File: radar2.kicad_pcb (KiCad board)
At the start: 4 copper layers, 103.4 x 65 mm, 135 parts, among them IC1 BQ25713RSNR, IC2 TPS54540DDA, IC3 LP5907QMFX-3.0Q1, IC5 LP5907QMFX-3.0Q1, IC6 DW3220TR13, J1 GSB1C4621DS1HR, J2 M20-8770546 (for SWD), J3 M20-9730446_DISPLAY_POWER, J4 JST-XH, J5 M20-9990646_PI, J6 SMA_CONNECTOR, J7 SMA_CONNECTOR, Q1 CSD17308Q3, Q2 CSD17308Q3, Q3 CSD17308Q3, Q4 CSD17308Q3, Q5 CSD25404Q3, SW1 09.03290.01, SW2 SWT0220-016016GSA, U1 STM32H725ZETx, Y1 ECS-384-CDX-2482

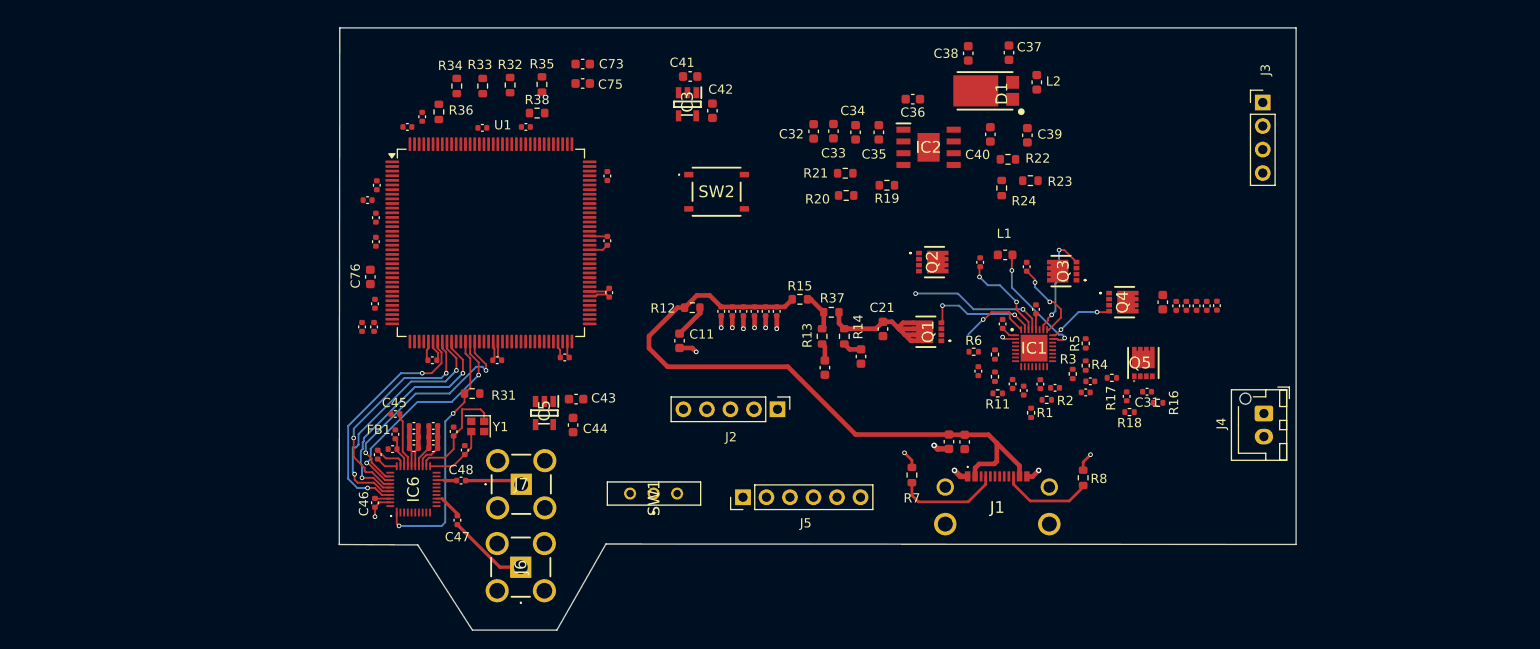
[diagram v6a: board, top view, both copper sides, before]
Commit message: replacing battery charger inductor with the correct one capable of handling high current applications, updating user footprint lib. Doing some serious routing leaving the battery charger for last due to complexity
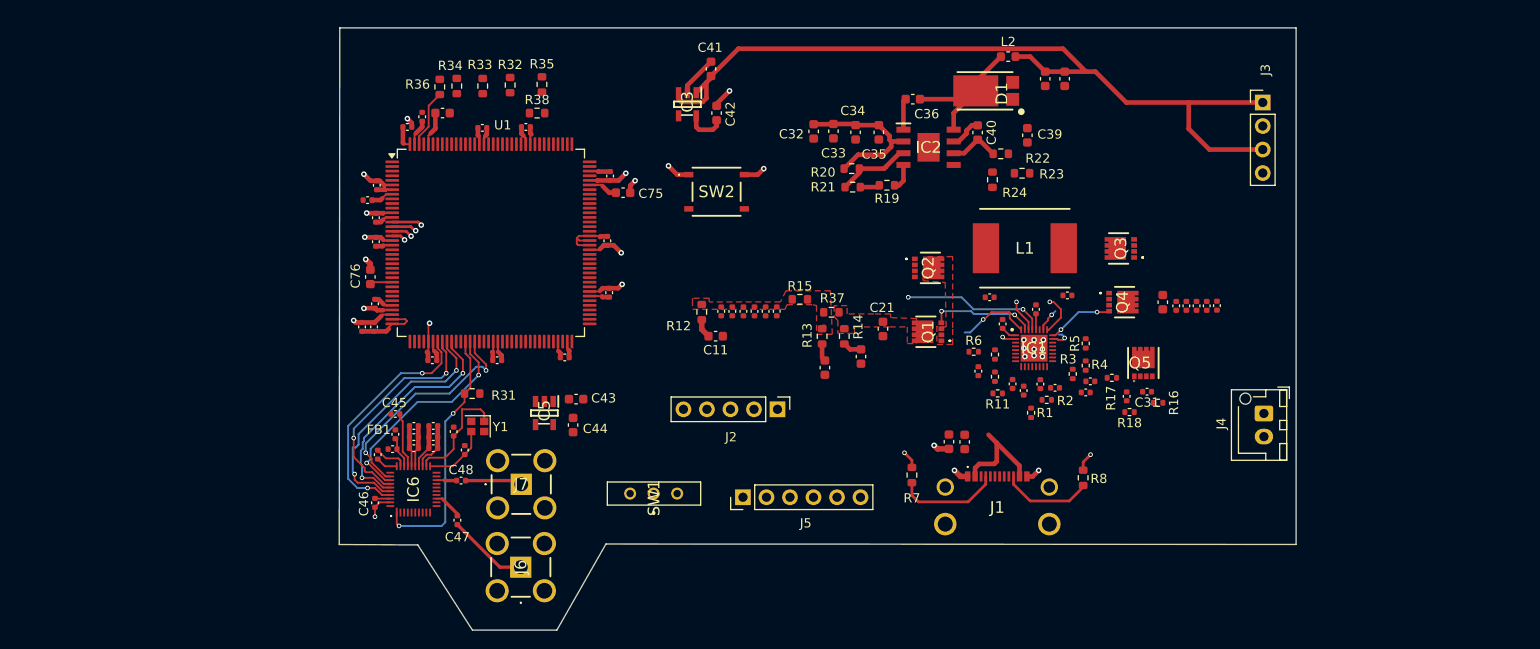
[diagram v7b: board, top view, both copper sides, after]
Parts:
- L1: footprint Inductor_SMD:L_0603_1608Metric -> induct:INDPM9785X300N
- moved C73 16.0 mm to (107.6, 68.0)
- moved C75 12.6 mm to (127.1, 76.6)
- moved C38 8.76 mm to (172.7, 64.3)
- moved Q3 6.69 mm to (180.9, 82.6)
- moved C37 6.64 mm to (174.8, 64.3), turned to 90 degrees
- moved C23 5.38 mm to (175.1, 87.7), turned to 0 degrees
- moved L2 4.15 mm to (168.7, 61.9), turned to 0 degrees
- moved C11 3.93 mm to (137.1, 92.1), turned to 0 degrees
- moved C22 3.92 mm to (166.7, 87.9), turned to 180 degrees
- moved R20 2.96 mm to (151.8, 74.0)
- moved R36 2.70 mm to (107.3, 65.2)
- moved C41 2.40 mm to (136.6, 63.2), turned to -90 degrees
- moved L1 2.24 mm to (170.5, 82.6)
- moved R21 1.70 mm to (151.9, 76.0)
- moved C40 1.39 mm to (165.4, 70.1)
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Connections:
- Q4 pad 5: GND -> /pmics/VSYS
- Q4 pad 6: GND -> /pmics/VSYS
- Q4 pad 7: GND -> /pmics/VSYS
- Q4 pad 8: GND -> /pmics/VSYS
- Q4 pad 9: GND -> /pmics/VSYS
- Q5 pad 5: GND -> /pmics/VSYS
- Q5 pad 6: GND -> /pmics/VSYS
- Q5 pad 7: GND -> /pmics/VSYS
- Q5 pad 8: GND -> /pmics/VSYS
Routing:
- net VOUT_5V: track 0.00 -> 91.4 mm
- net VBUS: track 77.3 -> 13.4 mm
- net GND: track 43.9 -> 93.9 mm, vias 13 -> 34
- net 3V3_MCU: track 10.5 -> 43.3 mm
- net /pmics/VSYS: track 0.00 -> 17.4 mm
- net /pmics/SW_1: track 0.00 -> 16.4 mm
- net Net-(Q1-D_1): track 15.1 -> 0.00 mm
- net /pmics/SW2: track 13.0 -> 2.26 mm, vias 2 -> 1
- net /pmics/LODRV2: track 11.7 -> 2.54 mm, vias 2 -> 1
- net Net-(IC2-EN): track 0.00 -> 8.10 mm
- net Net-(C73-Pad1): track 0.00 -> 6.85 mm
- net Net-(U1-PDR_ON): track 0.00 -> 6.28 mm
- net /pmics/BTST1: track 9.79 -> 3.54 mm, vias 2 -> 1
- net Net-(IC2-COMP): track 0.00 -> 5.50 mm
- net /pmics/BTST2: track 8.83 -> 4.47 mm, vias 2 -> 1
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- added copper zone on F.Cu, net /pmics/SW1
- added copper zone on F.Cu, net Net-(Q1-D_1)
- added copper zone on F.Cu, net VBUS

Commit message: routing power, for mcu and radar, leaving the BQ for lass still
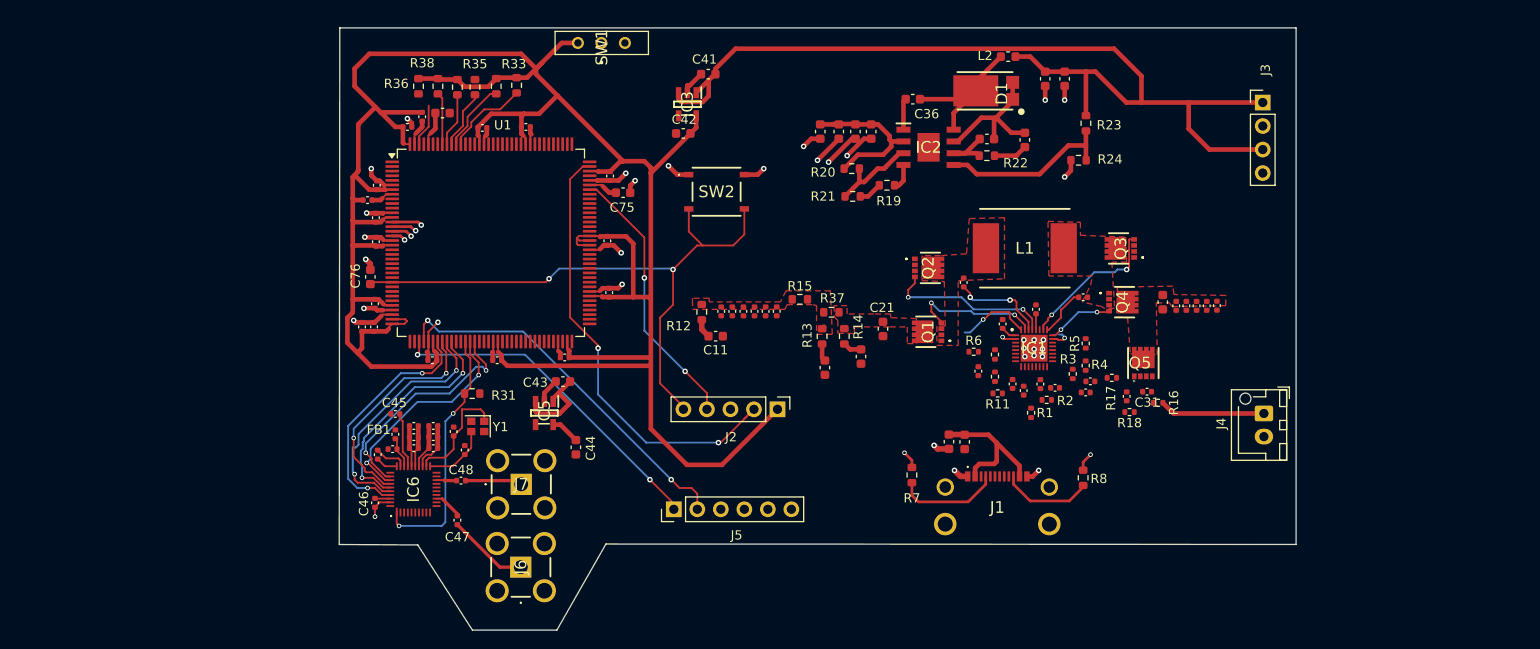
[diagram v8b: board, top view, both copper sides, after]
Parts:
- moved SW1 49.0 mm to (124.8, 60.4)
- moved R38 11.1 mm to (107.1, 65.1), turned to -90 degrees
- moved R24 9.53 mm to (176.3, 73.1), turned to 180 degrees
- moved R23 8.76 mm to (177.1, 69.1), turned to -90 degrees
- moved J5 7.58 mm to (132.6, 110.8)
- moved R35 7.24 mm to (111.1, 65.2)
- moved C42 4.22 mm to (133.6, 70.2), turned to 0 degrees
- moved R33 3.66 mm to (115.6, 65.0)
- moved C22 3.22 mm to (163.9, 86.3), turned to 90 degrees
- moved C44 2.42 mm to (122.0, 104.1), turned to 90 degrees
- moved C43 2.38 mm to (120.6, 97.0), turned to 0 degrees
- moved R36 2.30 mm to (105.0, 65.1)
- moved C23 1.71 mm to (176.8, 87.9)
- moved R22 1.51 mm to (166.4, 72.6)
- moved R32 1.51 mm to (113.4, 65.1)
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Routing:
- net 3V3_MCU: track 43.3 -> 269.2 mm
- net ST_NRST: track 2.45 -> 66.8 mm, vias 0 -> 2
- net ST_JTCLK: track 0.00 -> 49.2 mm, vias 0 -> 2
- net SW_USART2_RX: track 0.00 -> 41.0 mm, vias 0 -> 2
- net SW_USART2_TX: track 0.00 -> 36.5 mm, vias 0 -> 2
- net GND: track 93.9 -> 124.3 mm, vias 34 -> 40
- net ST_JTMS/SWDIO: track 0.00 -> 29.4 mm, vias 0 -> 2
- net VOUT_5V: track 91.4 -> 115.7 mm
- net /pmics/FB1: track 0.00 -> 19.2 mm
- net /pmics/LODRV2: track 2.54 -> 16.0 mm, vias 1 -> 2
- net BATT+: track 0.00 -> 11.4 mm
- net BQ_SCL: track 0.00 -> 9.04 mm
- net BQ_SDA: track 0.00 -> 7.59 mm
- net /pmics/BTST1: track 3.54 -> 10.2 mm, vias 1 -> 2
- net Net-(U1-BOOT0): track 0.00 -> 6.38 mm
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- added copper zone on F.Cu, net /pmics/SW2
- added copper zone on F.Cu, net /pmics/VSYS
